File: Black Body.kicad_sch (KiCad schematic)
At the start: 36 parts, among them IC2 MCP96L00T-E_MX, J1 53307-2471, J2 Conn_01x02, J3 Conn_01x04, J4 Conn_02x08_Top_Bottom, J5 Conn_01x06

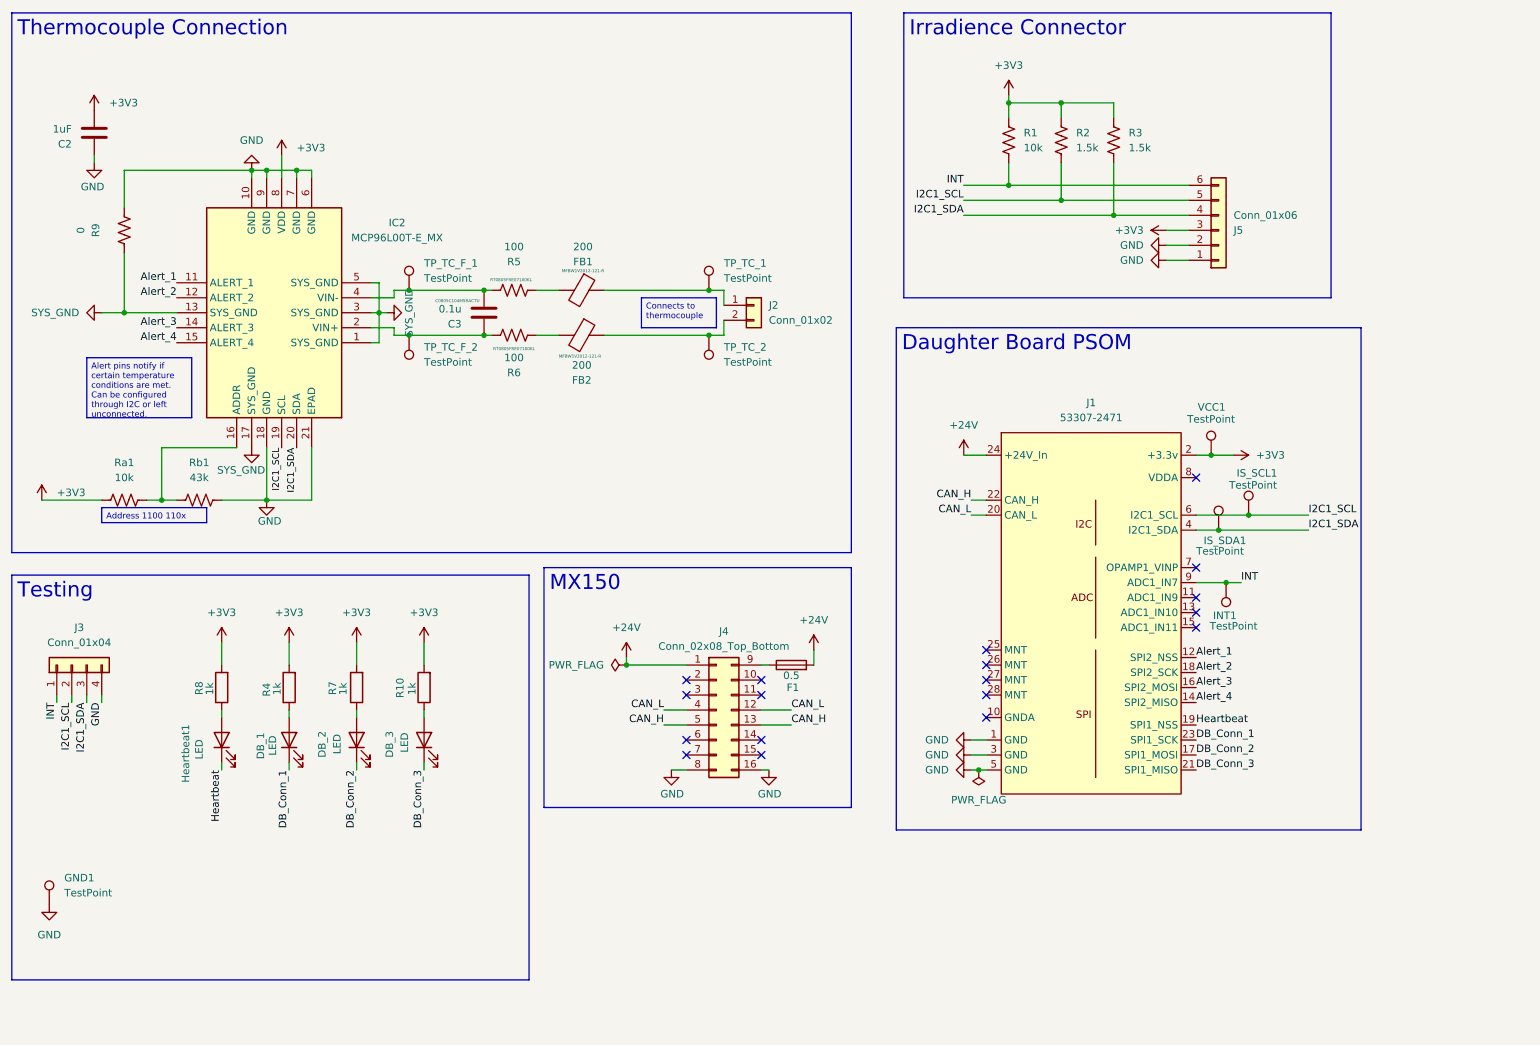
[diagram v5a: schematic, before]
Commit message: updated layout
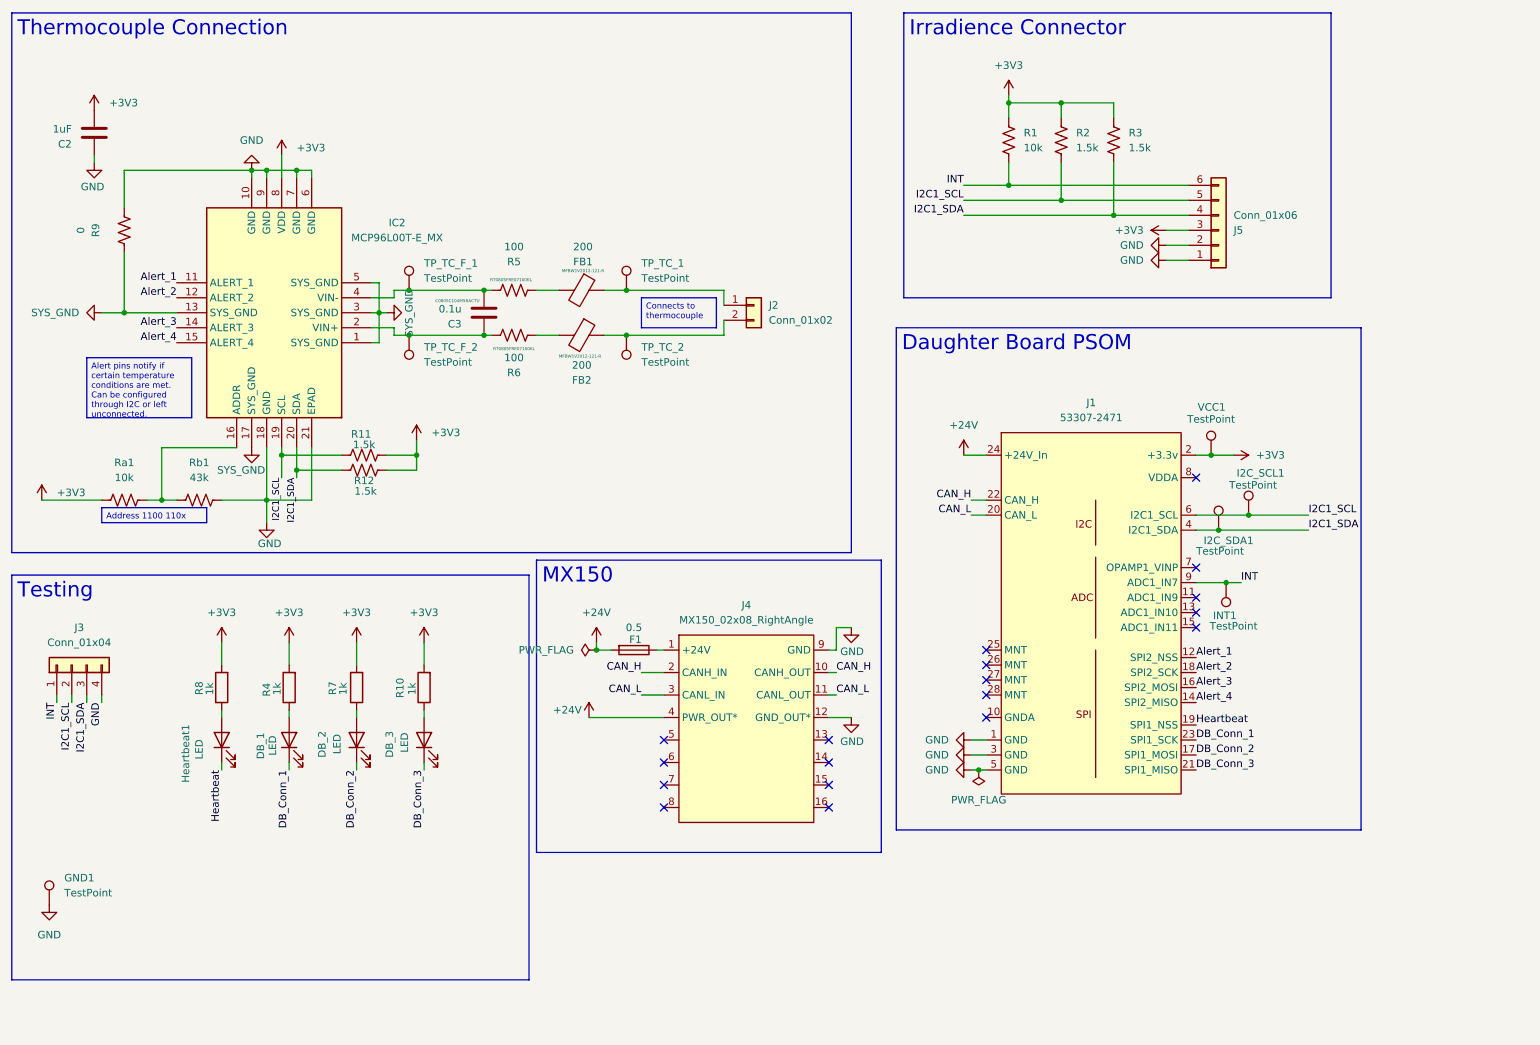
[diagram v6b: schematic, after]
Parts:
- removed J4: Conn_02x08_Top_Bottom, UTSVT_Connectors:CONN_SD-75900-001_2X08_MOL, symbol Connector_Generic:Conn_02x08_Top_Bottom
- added J4: MX150_02x08_RightAngle, UTSVT-Conn:CONN_SD-75900-001_2X08_MOL, symbol utsvt_connectors:MX150_02x08_RightAngle
- added R11, R12: 1.5k, Resistor_SMD:R_0805_2012Metric, symbol Device:R_US
- F1: footprint Fuse:Fuse_0603_1608Metric_Pad1.05x0.95mm_HandSolder -> Fuse:Fuseholder_Blade_Mini_Keystone_3568
- J1: footprint UTSVT_Connectors:PeripheralSOM -> UTSVT-Conn:PeripheralSOM
- renumbered IS_SCL1 to I2C_SCL1, IS_SDA1 to I2C_SDA1
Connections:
- net +24V: now also J4.4 (PWR_OUT*)
- net +3V3: now also R11.2, R12.2
- net CAN_H: now also J4.10 (CANH_OUT), J4.2 (CANH_IN)
- net CAN_L: now also J4.11 (CANL_OUT), J4.3 (CANL_IN)
- net GND: now also J4.12 (GND_OUT*), J4.9 (GND)
- net I2C1_SCL: now also R11.1
- net I2C1_SDA: now also R12.1
- net at F1.1: now also J4.1 (+24V)
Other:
- moved on the sheet: F1, TP_TC_1, TP_TC_2

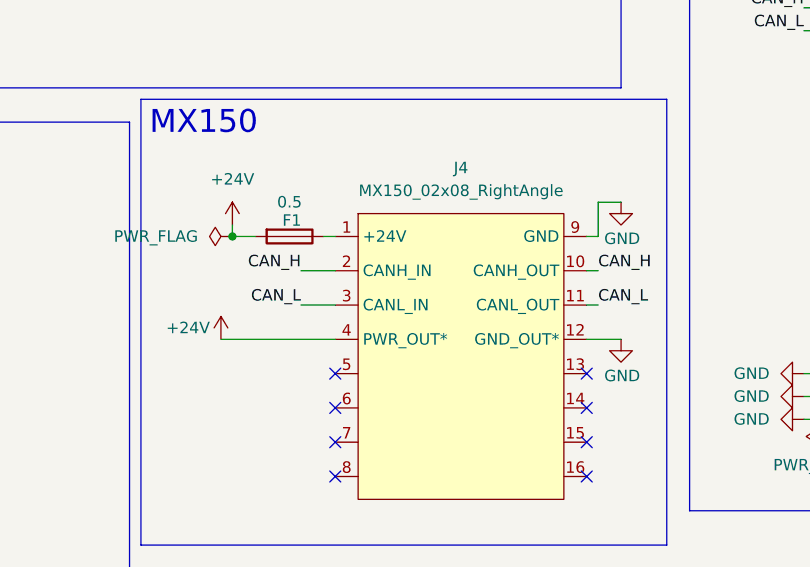
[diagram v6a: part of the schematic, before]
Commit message: updated connectors
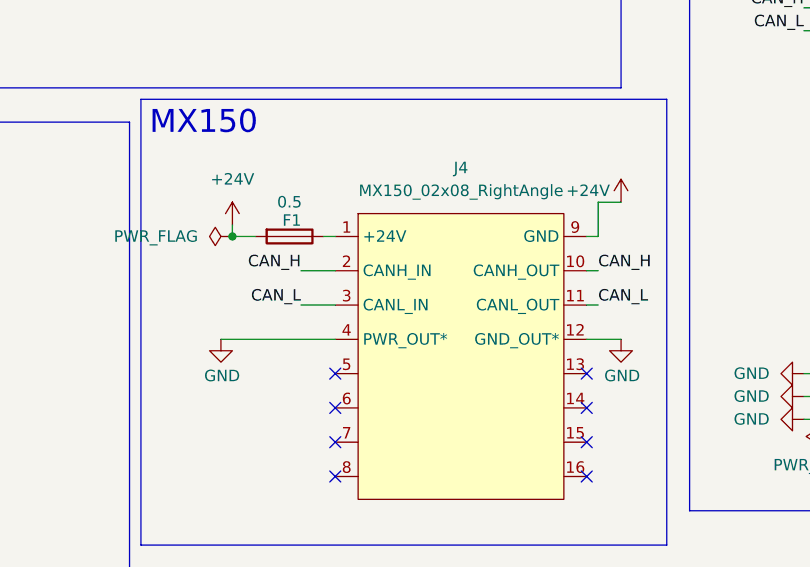
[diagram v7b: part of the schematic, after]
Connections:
- net +24V: now also J4.9 (GND); no longer J4.4 (PWR_OUT*)
- net GND: now also J4.4 (PWR_OUT*); no longer J4.9 (GND)
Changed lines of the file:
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@@
 	(symbol
 		(lib_id "power:+24V")
-		(at 114.3 133.35 0)
+		(at 158.75 118.11 0)
 		(unit 1)
 		(exclude_from_sim no)
@@
 		(dnp no)
 		(property "Reference" "#PWR012"
-			(at 114.3 137.16 0)
+			(at 158.75 121.92 0)
 			(effects
 				(font
@@
 		)
 		(property "Value" "+24V"
-			(at 108.204 132.08 0)
+			(at 152.654 116.84 0)
 			(effects
 				(font
@@
 		)
 		(property "Footprint" ""
-			(at 114.3 133.35 0)
+			(at 158.75 118.11 0)
 			(effects
 				(font
@@
 		)
 		(property "Datasheet" ""
-			(at 114.3 133.35 0)
+			(at 158.75 118.11 0)
 			(effects
 				(font
@@
 		)
 		(property "Description" "Power symbol creates a global label with name \"+24V\""
-			(at 114.3 133.35 0)
+			(at 158.75 118.11 0)
 			(effects
 				(font
@@
 	(symbol
 		(lib_id "power:GND")
-		(at 158.75 118.11 0)
-		(mirror y)
-		(unit 1)
-		(exclude_from_sim no)
-		(in_bom yes)
-		(on_board yes)
-		(dnp no)
-		(property "Reference" "#PWR011"
-			(at 158.75 124.46 0)
-			(effects
-				(font
-					(size 1.27 1.27)
-				)
-				(hide yes)
-			)
-		)
-		(property "Value" "GND"
-			(at 158.877 122.174 0)
-			(effects
-				(font
-					(size 1.27 1.27)
-				)
-			)
-		)
-		(property "Footprint" ""
-			(at 158.75 118.11 0)
-			(effects
-				(font
-					(size 1.27 1.27)
-				)
-				(hide yes)
-			)
-		)
-		(property "Datasheet" ""
-			(at 158.75 118.11 0)
-			(effects
-				(font
-					(size 1.27 1.27)
-				)
-				(hide yes)
-			)
-		)
-		(property "Description" "Power symbol creates a global label with name \"GND\" , ground"
-			(at 158.75 118.11 0)
-			(effects
-				(font
-					(size 1.27 1.27)
-				)
-				(hide yes)
-			)
-		)
-		(pin "1"
-		)
-		(instances
-			(project "Black Body"
-				(path "/326551d7-59c6-4bc5-b0df-e38f608d8925"
-					(reference "#PWR011")
-					(unit 1)
-				)
-			)
-		)
-	)
-	(symbol
-		(lib_id "power:GND")
 		(at 179.07 137.16 270)
 		(unit 1)
@@
 					(unit 1)
 				)
+			)
+		)
+	)
+	(symbol
+		(lib_id "power:GND")
+		(at 114.3 133.35 0)
+		(mirror y)
+		(unit 1)
+		(exclude_from_sim no)
+		(in_bom yes)
+		(on_board yes)
+		(dnp no)
+		(property "Reference" "#PWR011"
+			(at 114.3 139.7 0)
+			(effects
+				(font
+					(size 1.27 1.27)
+				)
+				(hide yes)
+			)
+		)
+		(property "Value" "GND"
+			(at 114.427 137.414 0)
+			(effects
+				(font
+					(size 1.27 1.27)
+				)
+			)
+		)
+		(property "Footprint" ""
+			(at 114.3 133.35 0)
+			(effects
+				(font
+					(size 1.27 1.27)
+				)
+				(hide yes)
+			)
+		)
+		(property "Datasheet" ""
+			(at 114.3 133.35 0)
+			(effects
+				(font
+					(size 1.27 1.27)
+				)
+				(hide yes)
+			)
+		)
+		(property "Description" "Power symbol creates a global label with name \"GND\" , ground"
+			(at 114.3 133.35 0)
+			(effects
+				(font
+					(size 1.27 1.27)
+				)
+				(hide yes)
+			)
+		)
+		(pin "1"
+		)
+		(instances
+			(project "Black Body"
+				(path "/326551d7-59c6-4bc5-b0df-e38f608d8925"
+					(reference "#PWR011")
+					(unit 1)
+				)

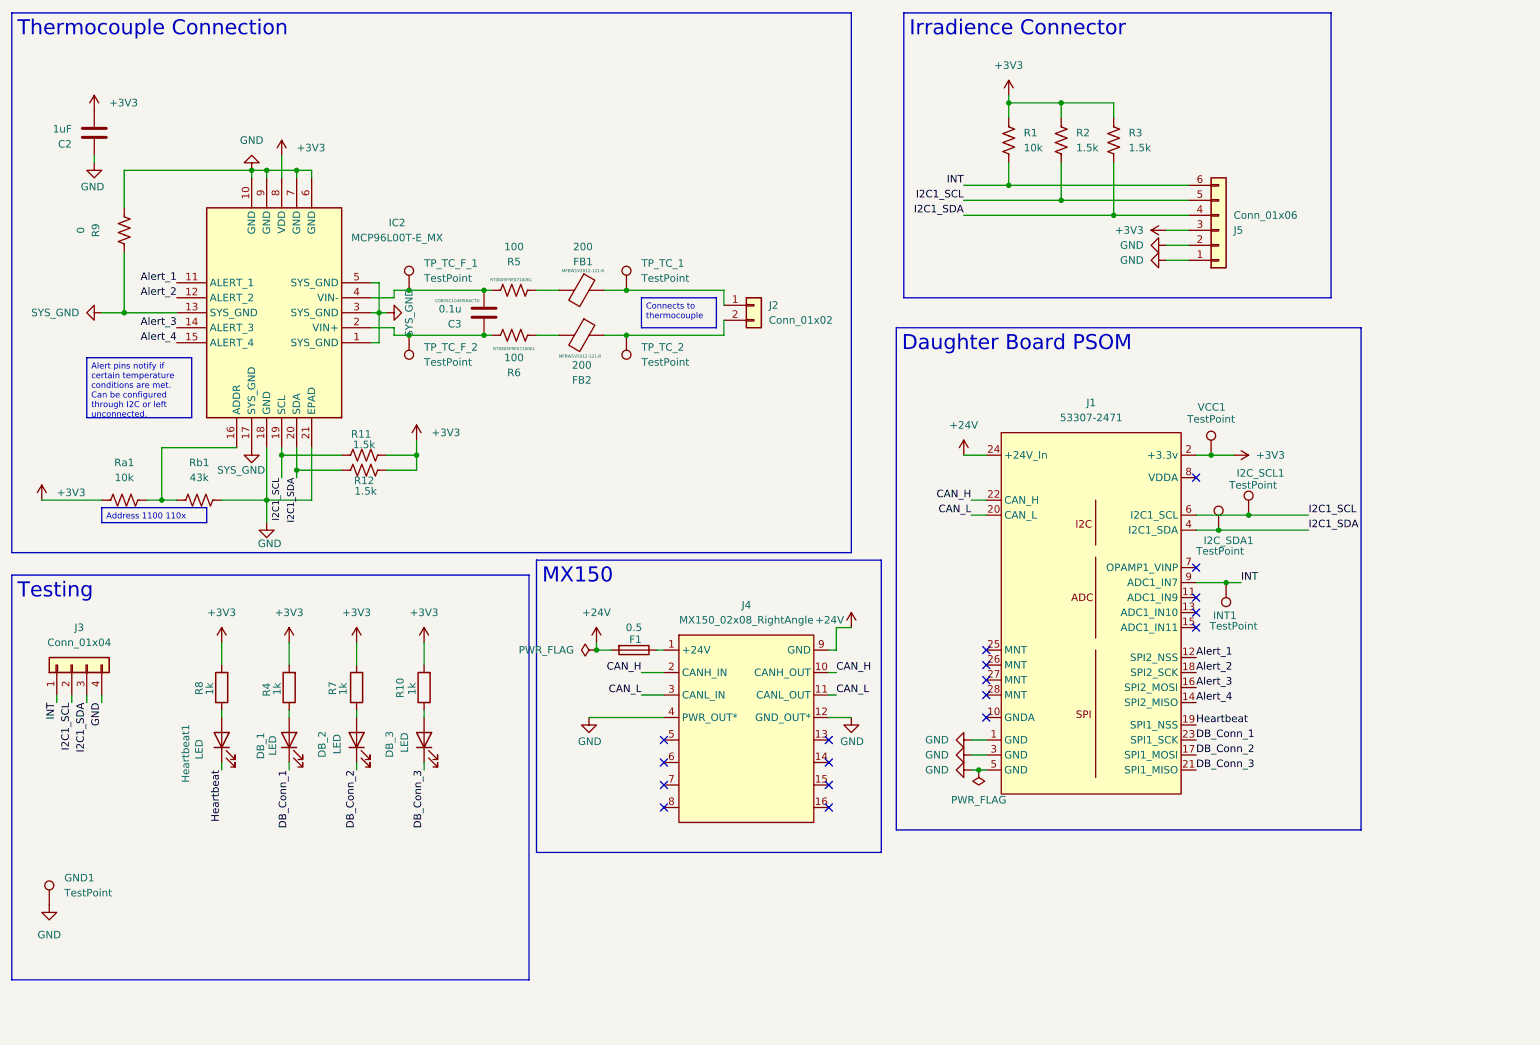
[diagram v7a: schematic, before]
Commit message: updated connectors
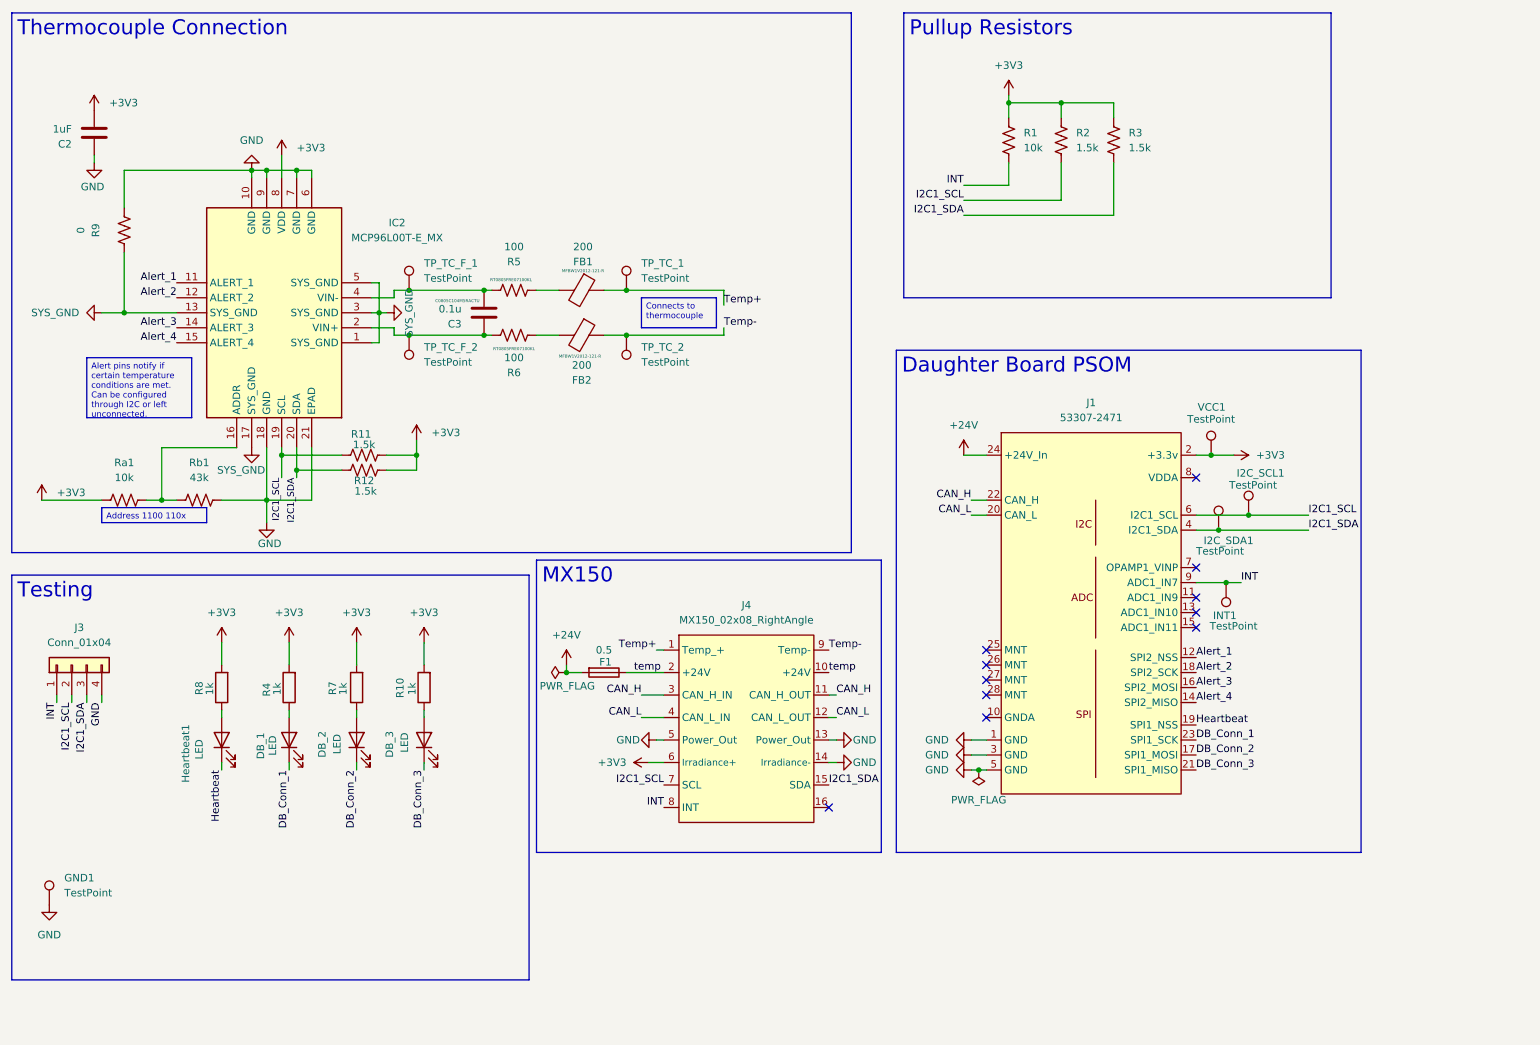
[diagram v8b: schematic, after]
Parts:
- removed J2: Conn_01x02, Connector_Molex:Molex_Nano-Fit_105313-xx02_1x02_P2.50mm_Horizontal, symbol Connector_Generic:Conn_01x02
- removed J5: Conn_01x06, Connector_Molex:Molex_Nano-Fit_105313-xx06_1x06_P2.50mm_Horizontal, symbol Connector_Generic:Conn_01x06
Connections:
- net +24V: no longer J4.9 (GND)
- net +3V3: now also J4.6 (Irradiance+)
- net CAN_H: now also J4.11 (CAN_H_OUT), J4.3 (CAN_H_IN); no longer J4.10 (CANH_OUT), J4.2 (CANH_IN)
- net CAN_L: now also J4.12 (CAN_L_OUT), J4.4 (CAN_L_IN); no longer J4.11 (CANL_OUT), J4.3 (CANL_IN)
- net GND: now also J4.13 (Power_Out), J4.14 (Irradiance-), J4.5 (Power_Out); no longer J4.12 (GND_OUT*), J4.4 (PWR_OUT*)
- net I2C1_SCL: now also J4.7 (SCL)
- net I2C1_SDA: now also J4.15 (SDA)
- net INT: now also J4.8 (INT)
- net Temp+: now reaches FB1.1, TP_TC_1.1
- net Temp+: now also J4.1 (Temp_+)
- net Temp-: now reaches FB2.1, TP_TC_2.1
- net Temp-: now also J4.9 (Temp-)
- net temp: now reaches F1.1
- net temp: now also J4.10 (+24V), J4.2 (+24V); no longer J4.1 (+24V)
- no-connect marks 18 -> 11
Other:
- moved on the sheet: F1
